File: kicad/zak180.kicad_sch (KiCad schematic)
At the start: 9 parts, among them U16 74HC00

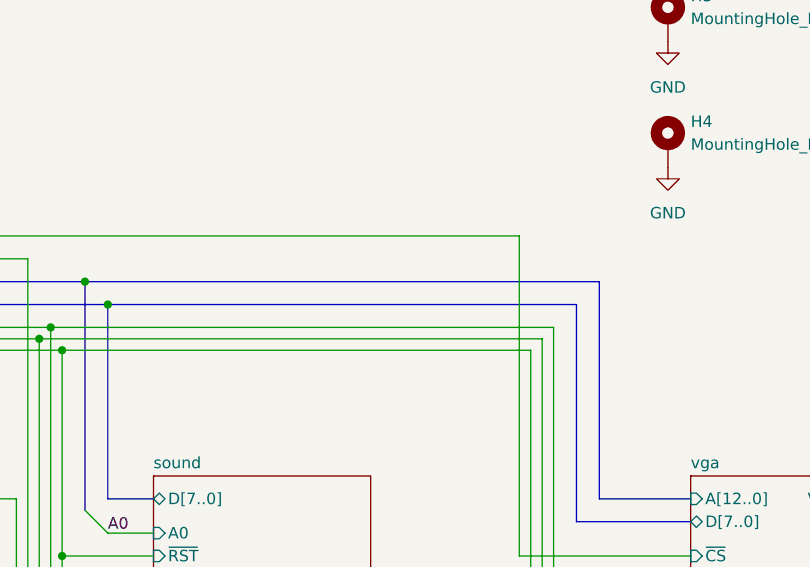
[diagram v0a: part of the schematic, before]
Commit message: HW: Fix A0 of AY-3-8912 being connected to D0 instead of A0
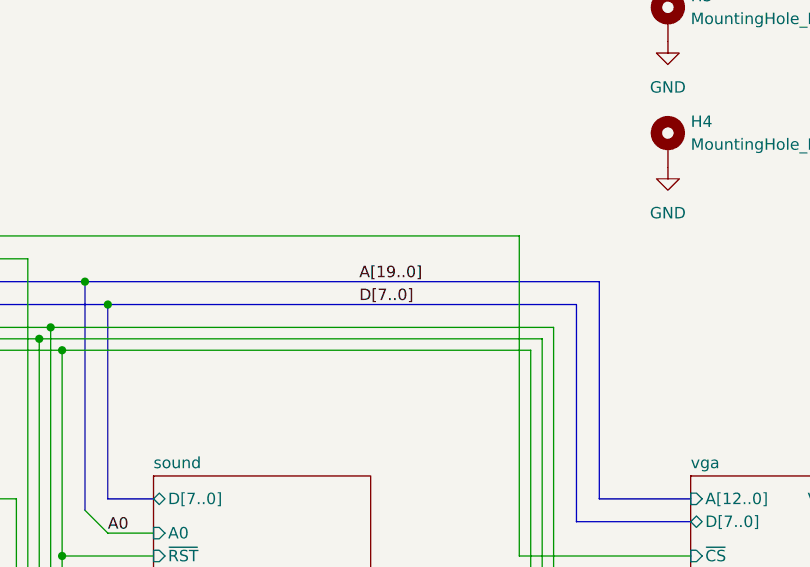
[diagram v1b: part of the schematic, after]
